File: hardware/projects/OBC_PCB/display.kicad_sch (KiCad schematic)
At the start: 9 parts, among them J1 LS021B7DD02, J6 Backlight A/K, Q1 AO3400A

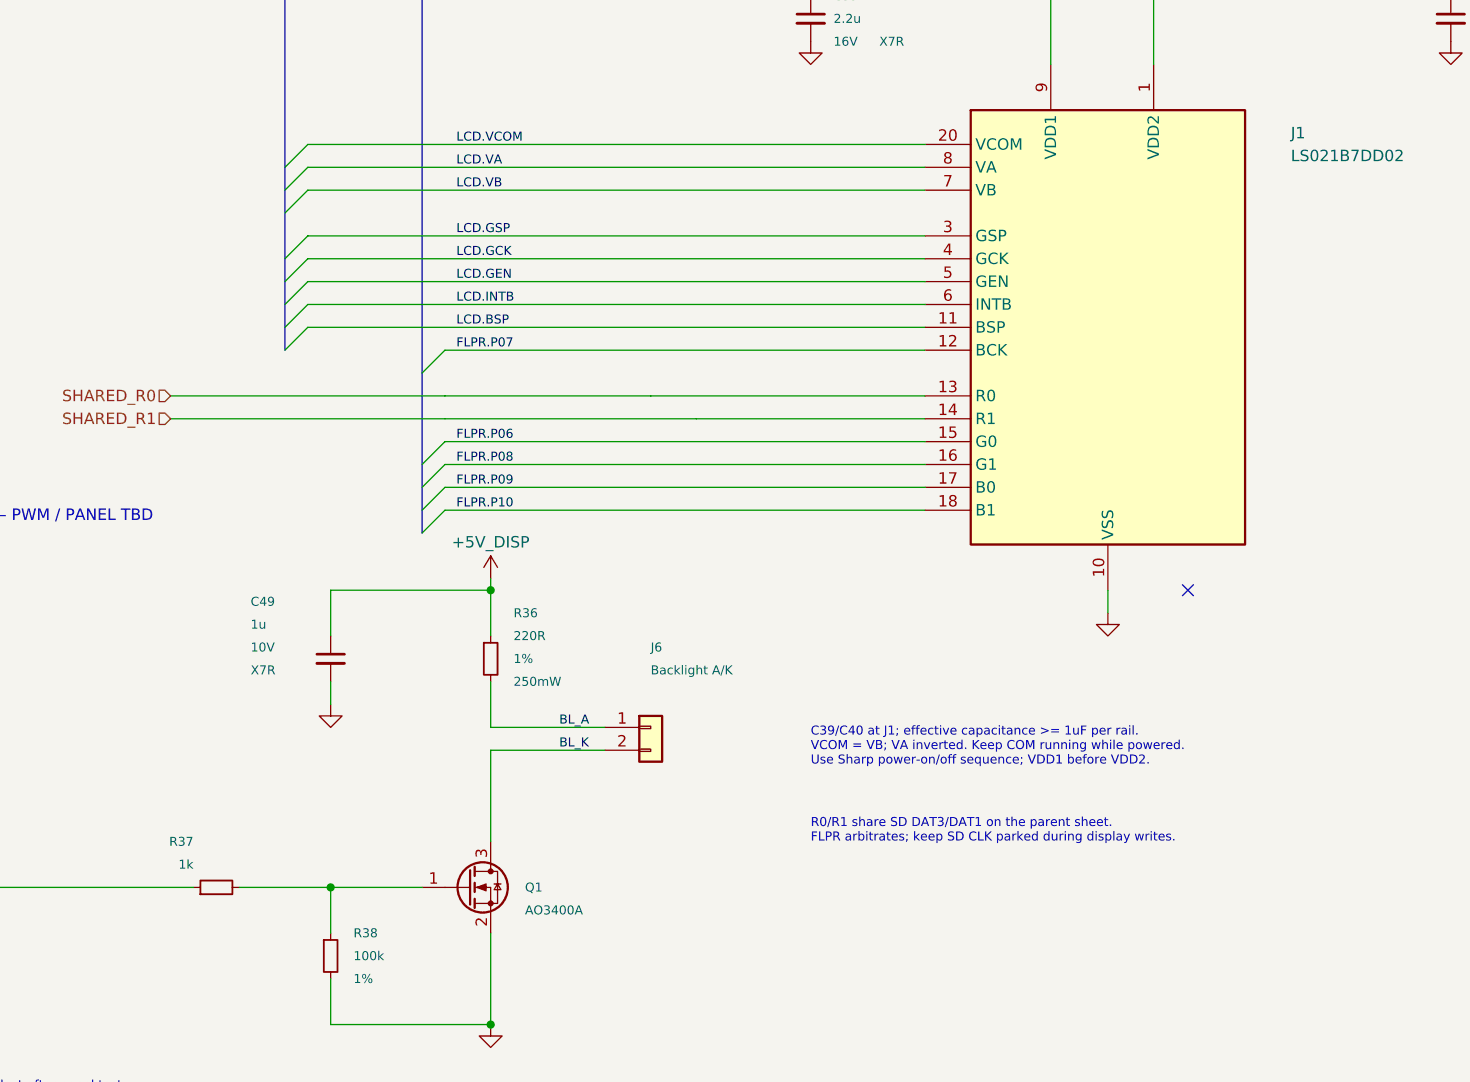
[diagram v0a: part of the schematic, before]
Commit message: fix(hardware): apply schematic review and peripheral pin mapping
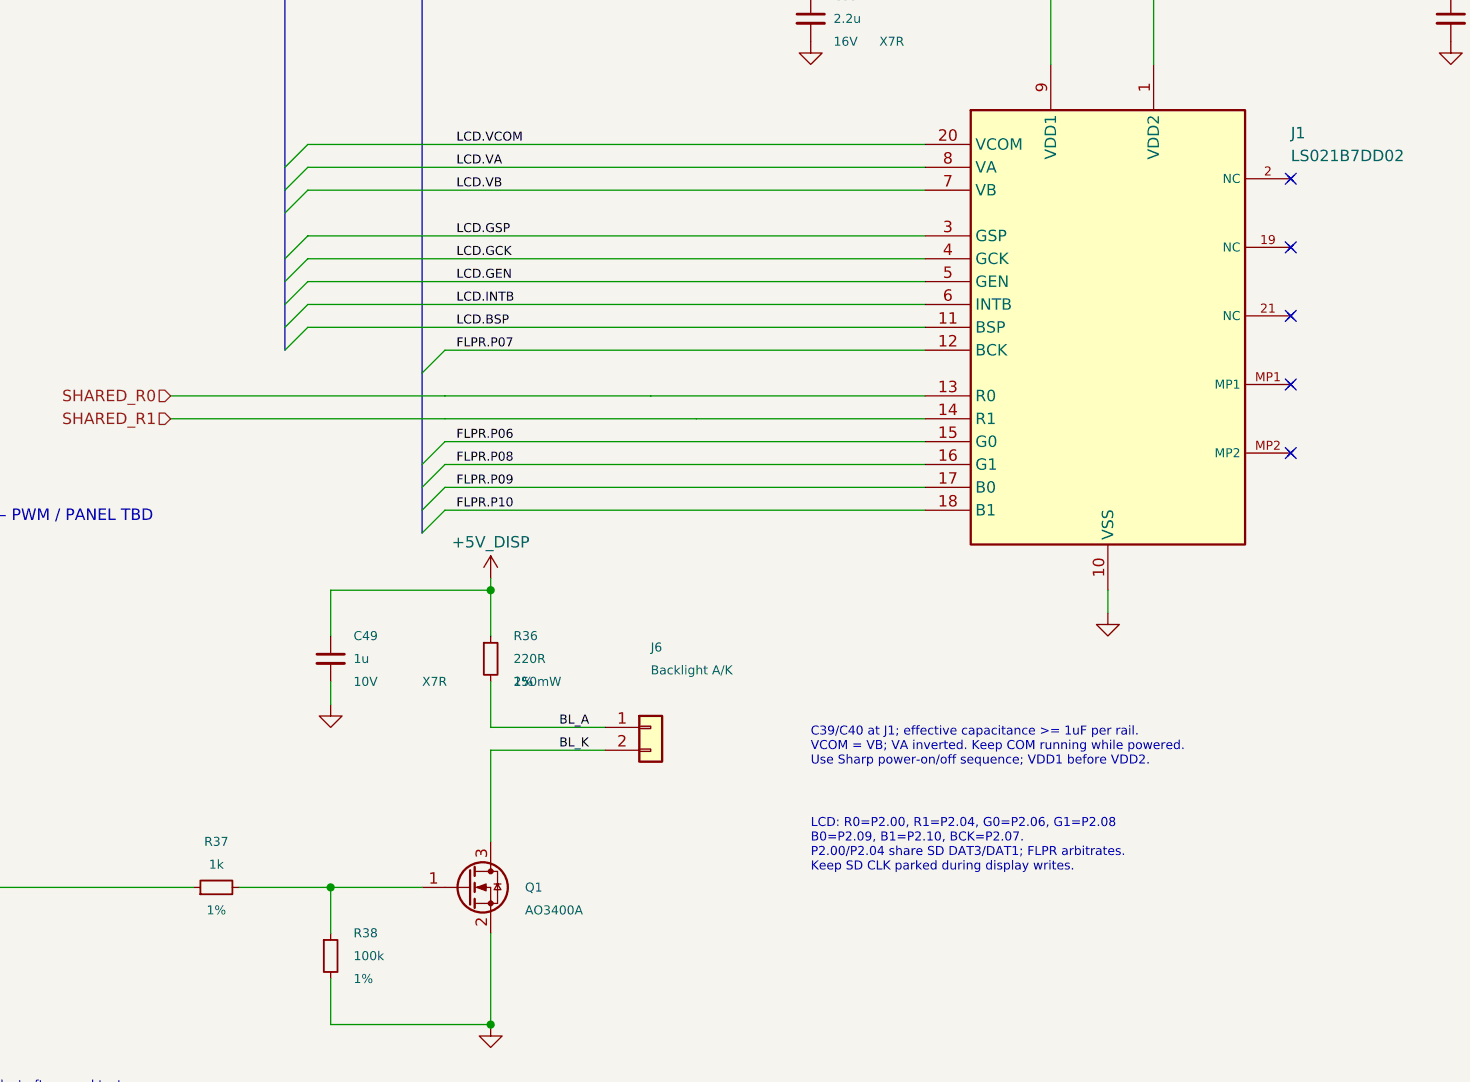
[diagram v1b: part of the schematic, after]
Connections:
- now unconnected: J1.19 (NC), J1.2 (NC), J1.21 (NC), J1.MP1, J1.MP2
- no-connect marks 1 -> 5
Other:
- note added: "LCD: R0=P2.00, R1=P2.04, G0=P2.06, G1=P2.08 B0=P2.09, B1=P2.10, BCK=P2.07. P2.00/P2.04 share SD DAT3/DAT1; FLPR arbitrates. Keep SD CLK parked during display writes."
- note removed: "R0/R1 share SD DAT3/DAT1 on the parent sheet. FLPR arbitrates; keep SD CLK parked during display writes."
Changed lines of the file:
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@@
 		)
-	)
-	(no_connect
-		(at 186.69 132.08)
 	)
 	(text "DISPLAY — LS021B7DD02 / 21-pin FPC"
@@
 		)
 	)
-	(text "R0/R1 share SD DAT3/DAT1 on the parent sheet.\nFLPR arbitrates; keep SD CLK parked during display writes."
+	(text "LCD: R0=P2.00, R1=P2.04, G0=P2.06, G1=P2.08\nB0=P2.09, B1=P2.10, BCK=P2.07.\nP2.00/P2.04 share SD DAT3/DAT1; FLPR arbitrates.\nKeep SD CLK parked during display writes."
 		(at 144.78 157.48 0)
 		(effects
@@
 		)
 		(property "Tolerance" "1%"
-			(at 111.76 139.7 0)
+			(at 111.76 142.23999999999998 0)
 			(effects
 				(font
@@
 		)
 		(property "Reference" "R36"
-			(at 111.76 134.62 0)
+			(at 111.76 137.16 0)
 			(effects
 				(font
@@
 		)
 		(property "Value" "220R"
-			(at 111.76 137.16 0)
+			(at 111.76 139.7 0)
 			(effects
 				(font
@@
 		)
 		(property "Tolerance" "1%"
-			(at 0 0 0)
-			(hide yes)
-			(effects
-				(font
-					(size 1.27 1.27)
-				)
-				(justify left)
+			(at 78.74 167.64 90)
+			(effects
+				(font
+					(size 1 1)
+				)
 			)
 		)
@@
 		)
 		(property "Reference" "R37"
-			(at 76.2 160.02 90)
-			(effects
-				(font
-					(size 1 1)
-				)
-				(justify left)
+			(at 78.74 160.01999999999998 90)
+			(effects
+				(font
+					(size 1 1)
+				)
 			)
 		)
 		(property "Value" "1k"
-			(at 76.2 162.56 90)
-			(effects
-				(font
-					(size 1 1)
-				)
-				(justify left)
+			(at 78.74 162.56 90)
+			(effects
+				(font
+					(size 1 1)
+				)
 			)
 		)
@@
 		)
 		(property "Voltage" "10V"
-			(at 82.55 138.43 0)
+			(at 93.98 142.24 0)
 			(effects
 				(font
@@
 		)
 		(property "Dielectric" "X7R"
-			(at 82.55 140.97 0)
+			(at 101.6 142.24 0)
 			(effects
 				(font
@@
 		)
 		(property "Reference" "C49"
-			(at 82.55 133.35 0)
+			(at 93.98 137.16 0)
 			(effects
 				(font
@@
 		)
 		(property "Value" "1u"
-			(at 82.55 135.89 0)
+			(at 93.98 139.7 0)
 			(effects
 				(font
@@
 		)
 	)
+	(no_connect
+		(at 198.12 86.36)
+	)
+	(no_connect
+		(at 198.12 93.98)
+	)
+	(no_connect
+		(at 198.12 101.6)
+	)
+	(no_connect
+		(at 198.12 109.22)
+	)
+	(no_connect
+		(at 198.12 116.84)
+	)
 )

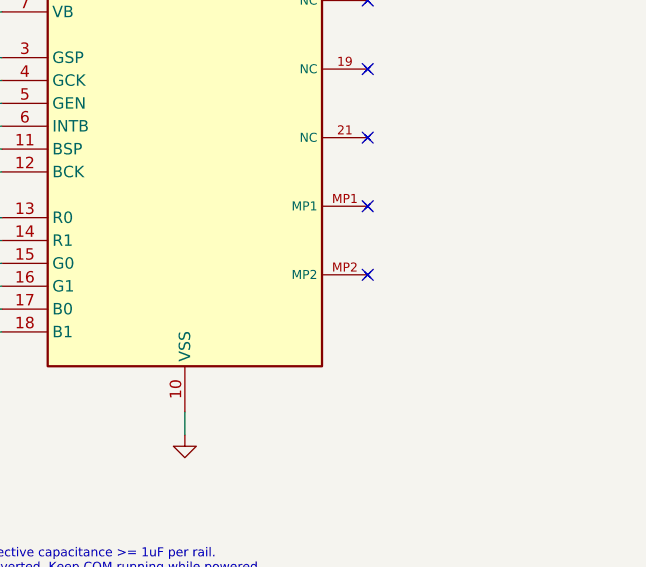
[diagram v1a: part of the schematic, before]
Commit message: hardware: name critical nets and ground connector tabs
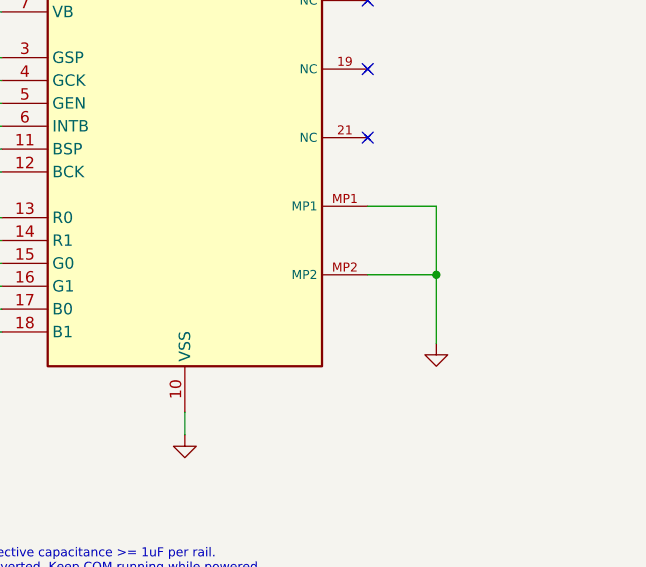
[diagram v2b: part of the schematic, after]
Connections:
- net GND: now also J1.MP1, J1.MP2
- no-connect marks 5 -> 3
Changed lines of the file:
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@@
 		(at 198.12 101.6)
 	)
-	(no_connect
-		(at 198.12 109.22)
+	(wire
+		(pts
+			(xy 198.12 109.22)
+			(xy 205.74 109.22)
+		)
+		(stroke
+			(width 0)
+			(type default)
+		)
 	)
-	(no_connect
-		(at 198.12 116.84)
+	(wire
+		(pts
+			(xy 205.74 109.22)
+			(xy 205.74 116.84)
+		)
+		(stroke
+			(width 0)
+			(type default)
+		)
+	)
+	(wire
+		(pts
+			(xy 205.74 116.84)
+			(xy 205.74 124.46)
+		)
+		(stroke
+			(width 0)
+			(type default)
+		)
+	)
+	(wire
+		(pts
+			(xy 198.12 116.84)
+			(xy 205.74 116.84)
+		)
+		(stroke
+			(width 0)
+			(type default)
+		)
+	)
+	(junction
+		(at 205.74 116.84)
+		(diameter 0)
+		(color 0 0 0 0)
+	)
+	(symbol
+		(lib_id "power:GND")
+		(at 205.74 124.46 0)
+		(unit 1)
+		(body_style 1)
+		(exclude_from_sim no)
+		(in_bom yes)
+		(on_board yes)
+		(in_pos_files yes)
+		(dnp no)
+		(fields_autoplaced yes)
+		(property "Reference" "#PWR2403"
+			(at 208.28 120.65 0)
+			(hide yes)
+			(show_name no)
+			(do_not_autoplace no)
+			(effects
+				(font
+					(size 1.27 1.27)
+				)
+				(justify left)
+			)
+		)
+		(property "Value" "GND"
+			(at 208.28 121.92 0)
+			(hide yes)
+			(show_name no)
+			(do_not_autoplace no)
+			(effects
+				(font
+					(size 1.27 1.27)
+				)
+				(justify left)
+			)
+		)
+		(property "Footprint" ""
+			(at 208.28 123.19 0)
+			(hide yes)
+			(show_name no)
+			(do_not_autoplace no)
+			(effects
+				(font
+					(size 1.27 1.27)
+				)
+				(justify left)
+			)
+		)
+		(property "Datasheet" "~"
+			(at 208.28 124.46 0)
+			(hide yes)
+			(show_name no)
+			(do_not_autoplace no)
+			(effects
+				(font
+					(size 1.27 1.27)
+				)
+				(justify left)
+			)
+		)
+		(property "Description" ""
+			(at 208.28 125.73 0)
+			(hide yes)
+			(show_name no)
+			(do_not_autoplace no)
+			(effects
+				(font
+					(size 1.27 1.27)
+				)
+				(justify left)
+			)
+		)
+		(pin "1"
+		)
+		(instances
+			(project "OBC_PCB"
+				(path "/57e91c39-b072-457b-b097-52c5b44e61c8/6b8cca09-5e52-4203-8b94-2412467f33a4"
+					(reference "#PWR2403")
+					(unit 1)
+				)
+			)
+		)
 	)
 )

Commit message: hardware: prepare QFN schematic for non-HDI boards
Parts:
- removed Q1: AO3400A, Package_TO_SOT_SMD:SOT-23, symbol Transistor_FET:AO3400A
- removed R36: 220R, Resistor_SMD:R_0805_2012Metric, symbol Device:R_Small
- removed R37: 1k, Resistor_SMD:R_0402_1005Metric, symbol Device:R_Small
- removed R38: 100k, Resistor_SMD:R_0402_1005Metric, symbol Device:R_Small
- added C53: 100n, Capacitor_SMD:C_0402_1005Metric, symbol Device:C_Small
- added C54: 1u, Capacitor_SMD:C_0603_1608Metric, symbol Device:C_Small
- added R46: 47k, Resistor_SMD:R_0402_1005Metric, symbol Device:R_Small
- added R47, R51, R52, R53, R54, R55, R56, R57, R58, R59, R60, R61, R62: 100k, Resistor_SMD:R_0402_1005Metric, symbol Device:R_Small
- added R48, R49: 150R, Resistor_SMD:R_0402_1005Metric, symbol Device:R_Small
- added R50: 0R, Resistor_SMD:R_0402_1005Metric, symbol Device:R_Small
- added U8: SN74LVC02APWR, Package_SO:TSSOP-14_4.4x5mm_P0.65mm, symbol obc:SN74LVC02APWR
- added U9: LP5810BDSDR, obc:LP5810_DSD0008B, symbol obc:LP5810BDSDR
- C49: value 1u -> 2.2u; footprint Capacitor_SMD:C_0402_1005Metric -> Capacitor_SMD:C_0603_1608Metric; Capacitance at bias Minimum 0.5uF at 5V over tolerance and temperature -> >=1uF at 3.36V
- J6: value Backlight A/K -> BACKLIGHT A/K - TBD
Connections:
- net BL_A is gone; now on net +5V_DISP: J6.1 (Pin_1)
- net +3V2: now also C49.1, C53.1, C54.1, U8.14 (VCC), U9.1 (VCC)
- net +5V_DISP: no longer C49.1
- net BL_K: now also U9.8 (OUT0)
- net GND: now also C53.2, C54.2, R46.2, R47.2, R51.2, R52.2, R53.2, R54.2, R55.2, R56.2, R57.2, R58.2, R59.2, R60.2, R61.2, R62.2, U8.3, U8.6, U8.7 (GND), U9.2 (SYNC), U9.9 (GND)
- net FLPR.P06 renamed LCD_G0
- net LCD_G0: now also R53.1
- net FLPR.P07 renamed LCD_BCK
- net LCD_BCK: now also R62.1
- net FLPR.P08 renamed LCD_G1
- net LCD_G1: now also R54.1
- net FLPR.P09 renamed LCD_B0
- net LCD_B0: now also R55.1
- net FLPR.P10 renamed LCD_B1
- net LCD_B1: now also R56.1
- net LCD.BSP renamed LCD_BSP
- net LCD_BSP: now also R61.1
- net LCD.GCK renamed LCD_GCK
- net LCD_GCK: now also R59.1
- net LCD.GEN renamed LCD_GEN
- net LCD_GEN: now also R58.1
- net LCD.GSP renamed LCD_GSP
- net LCD_GSP: now also R57.1
- net LCD.INTB renamed LCD_INTB
- net LCD_INTB: now also R60.1
- net LCD.VA: no longer names the net of J1.8 (VA)
- net LCD.VA: now also R49.2
- net LCD.VB: no longer names the net of J1.7 (VB)
- net LCD.VB: now also R50.2
- net LCD.VCOM: no longer names the net of J1.20 (VCOM)
- net LCD.VCOM: now also R48.2, R50.1
- net SHARED_R0 renamed LCD_R0
- net LCD_R0: now also R51.1
- net SHARED_R1 renamed LCD_R1
- net LCD_R1: now also R52.1
- new net: U8.12, U8.4, U8.9
- new net: U8.1, U8.8
- new net: R48.1, U8.10
- new net: R49.1, U8.13
- new net COM_EN: R47.1, U8.5
- new net COM_SOURCE: R46.1, U8.11, U8.2
- new net SCL: U9.3 (SCL)
- new net SDA: U9.4 (SDA)
- no-connect marks 3 -> 6
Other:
- note added: "0x54-0x57; SYNC low. PWM = 255; use DC brightness. Keep lsd_action = 0 on 3.2V (possible false short flags). OUT1-3 spare. LED load and J6 footprint remain unresolved."
- note added: "ALL 12 DIGITAL INPUTS HAVE RESET PULL-DOWNS C39/C40: >=1uF effective. R50 at J1 joins VB to VCOM after R48."
- note added: "BACKLIGHT / I2C CURRENT SINK"
- note added: "COM_EN = 0: VA, VB and VCOM low. COM_EN = 1: VCOM = VB = Q; VA = inverse Q. 60Hz, 50% duty; verify electrode edges at J1."
- note added: "LCD ELECTRODES / FAIL-LOW ENABLE"
- note added: "PMIC GPIO survives MCU reset. Clear COM_EN first at boot, before planned reset and shutdown. Unexpected resets still need DC-bias qualification; this is not a reset interlock."
- note removed: "220R: ~9mA at Vf=3.0V; select after panel test. Single-Vf panel; parallel branches need ballast in panel. PWM active high; idle low. Enable 5V before PWM."
- note removed: "BACKLIGHT — PWM / PANEL TBD"
- note removed: "C39/C40 at J1; effective capacitance >= 1uF per rail. VCOM = VB; VA inverted. Keep COM running while powered. Use Sharp power-on/off sequence; VDD1 before VDD2."
- note removed: "DISPLAY — LS021B7DD02 / 21-pin FPC"
- note removed: "LCD: R0=P2.00, R1=P2.04, G0=P2.06, G1=P2.08 B0=P2.09, B1=P2.10, BCK=P2.07. P2.00/P2.04 share SD DAT3/DAT1; FLPR arbitrates. Keep SD CLK parked during display writes."
- title: OpenBikeComputer — Display -> OpenBikeComputer - display and backlight
- moved on the sheet: C39, C40, C49, J1, J6
